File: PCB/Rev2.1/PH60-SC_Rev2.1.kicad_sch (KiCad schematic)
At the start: 48 parts, among them J1 USB_C_Receptacle_USB2.0_14P, J2 Conn_01x02_Pin, J3 Conn_01x02_Pin, U1 nRF52840, U5 LIS2DE12, X1 32.768kHz, X2 Crystal_Generic

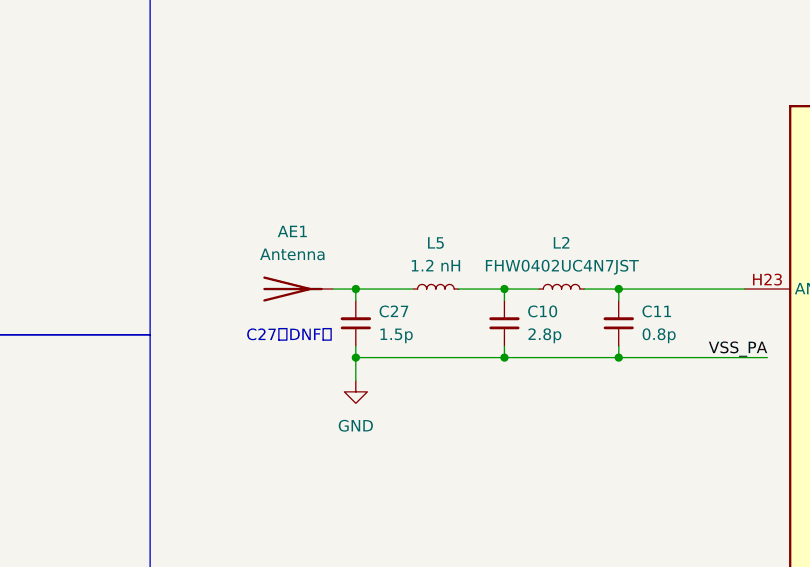
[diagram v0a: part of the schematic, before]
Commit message: 天线设计回退至sc2生产版本
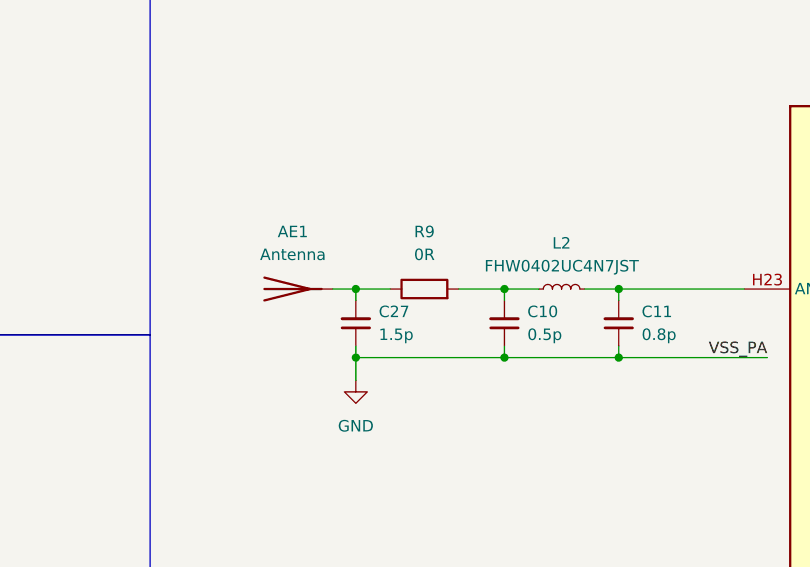
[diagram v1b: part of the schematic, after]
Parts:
- removed L5: 1.2 nH, Inductor_SMD:L_0402_1005Metric, symbol Device:L_Small
- added R9: 0R, Capacitor_SMD:C_0402_1005Metric, symbol Device:R
- C10: value 2.8p -> 0.5p
- C27: now in the parts list
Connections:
- net at AE1.1 (A), C27.2: now also R9.1
- net at C10.2, L2.1: now also R9.2
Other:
- note removed: "C27（DNF）"
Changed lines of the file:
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@@
 		)
 	)
-	(text "C27（DNF）"
-		(exclude_from_sim no)
-		(at 124.714 78.994 0)
-		(effects
-			(font
-				(size 1.27 1.27)
-			)
-		)
-	)
 	(text "ESD"
 		(exclude_from_sim no)
@@
 	)
 	(junction
+		(at 148.59 73.66)
+		(diameter 0)
+		(color 0 0 0 0)
+	)
+	(junction
 		(at 288.29 34.29)
 		(diameter 0)
@@
 		(color 0 0 0 0)
 	)
-	(junction
-		(at 148.59 73.66)
-		(diameter 0)
-		(color 0 0 0 0)
-	)
 	(no_connect
 		(at 241.3 101.6)
@@
 	(wire
 		(pts
-			(xy 143.51 73.66) (xy 148.59 73.66)
-		)
-		(stroke
-			(width 0)
-			(type default)
-		)
-	)
-	(wire
-		(pts
 			(xy 166.37 162.56) (xy 175.26 162.56)
 		)
@@
 	(wire
 		(pts
+			(xy 143.51 73.66) (xy 148.59 73.66)
+		)
+		(stroke
+			(width 0)
+			(type default)
+		)
+	)
+	(wire
+		(pts
 			(xy 298.45 41.91) (xy 298.45 45.72)
 		)
@@
 	(wire
 		(pts
+			(xy 132.08 73.66) (xy 135.89 73.66)
+		)
+		(stroke
+			(width 0)
+			(type default)
+		)
+	)
+	(wire
+		(pts
 			(xy 248.92 182.88) (xy 257.81 182.88)
 		)
@@
 	(wire
 		(pts
-			(xy 132.08 73.66) (xy 138.43 73.66)
-		)
-		(stroke
-			(width 0)
-			(type default)
-		)
-	)
-	(wire
-		(pts
 			(xy 213.36 35.56) (xy 213.36 48.26)
 		)
@@
 	)
 	(symbol
+		(lib_id "Device:R")
+		(at 139.7 73.66 90)
+		(unit 1)
+		(body_style 1)
+		(exclude_from_sim no)
+		(in_bom yes)
+		(on_board yes)
+		(in_pos_files yes)
+		(dnp no)
+		(fields_autoplaced yes)
+		(property "Reference" "R9"
+			(at 139.7 67.31 90)
+			(show_name no)
+			(do_not_autoplace no)
+			(effects
+				(font
+					(size 1.27 1.27)
+				)
+			)
+		)
+		(property "Value" "0R"
+			(at 139.7 69.85 90)
+			(show_name no)
+			(do_not_autoplace no)
+			(effects
+				(font
+					(size 1.27 1.27)
+				)
+			)
+		)
+		(property "Footprint" "Capacitor_SMD:C_0402_1005Metric"
+			(at 139.7 75.438 90)
+			(hide yes)
+			(show_name no)
+			(do_not_autoplace no)
+			(effects
+				(font
+					(size 1.27 1.27)
+				)
+			)
+		)
+		(property "Datasheet" ""
+			(at 139.7 73.66 0)
+			(hide yes)
+			(show_name no)
+			(do_not_autoplace no)
+			(effects
+				(font
+					(size 1.27 1.27)
+				)
+			)
+		)
+		(property "Description" "Resistor"
+			(at 139.7 73.66 0)
+			(hide yes)
+			(show_name no)
+			(do_not_autoplace no)
+			(effects
+				(font
+					(size 1.27 1.27)
+				)
+			)
+		)
+		(pin "2"
+		)
+		(pin "1"
+		)
+		(instances
+			(project "PH60-SC_Rev2.1"
+				(path "/dca0f898-8fdb-4522-a51d-f4f4238906e7"
+					(reference "R9")
+					(unit 1)
+				)
+			)
+		)
+	)
+	(symbol
 		(lib_id "Device:L_Small")
 		(at 283.21 30.48 0)
@@
 			)
 		)
-		(property "Value" "2.8p"
+		(property "Value" "0.5p"
 			(at 151.13 78.7335 0)
 			(show_name no)
@@
 		(body_style 1)
 		(exclude_from_sim no)
-		(in_bom no)
+		(in_bom yes)
 		(on_board yes)
 		(in_pos_files yes)
@@
 					(unit 1)
 				)
-			)
-		)
-	)
-	(symbol
-		(lib_id "Device:L_Small")
-		(at 140.97 73.66 90)
-		(unit 1)
-		(body_style 1)
-		(exclude_from_sim no)
-		(in_bom yes)
-		(on_board yes)
-		(in_pos_files yes)
-		(dnp no)
-		(fields_autoplaced yes)
-		(property "Reference" "L5"
-			(at 140.97 68.58 90)
-			(show_name no)
-			(do_not_autoplace no)
-			(effects
-				(font
-					(size 1.27 1.27)
-				)
-			)
-		)
-		(property "Value" "1.2 nH"
-			(at 140.97 71.12 90)
-			(show_name no)
-			(do_not_autoplace no)
-			(effects
-				(font
-					(size 1.27 1.27)
-				)
-			)
-		)
-		(property "Footprint" "Inductor_SMD:L_0402_1005Metric"
-			(at 140.97 73.66 0)
-			(hide yes)
-			(show_name no)
-			(do_not_autoplace no)
-			(effects
-				(font
-					(size 1.27 1.27)
-				)
-			)
-		)
-		(property "Datasheet" ""
-			(at 140.97 73.66 0)
-			(hide yes)
-			(show_name no)
-			(do_not_autoplace no)
-			(effects
-				(font
-					(size 1.27 1.27)
-				)
-			)
-		)
-		(property "Description" "Inductor, small symbol"
-			(at 140.97 73.66 0)
-			(hide yes)
-			(show_name no)
-			(do_not_autoplace no)
-			(effects
-				(font
-					(size 1.27 1.27)
-				)
-			)
-		)
-		(pin "2"
-		)
-		(pin "1"
-		)
-		(instances
-			(project "PH60-SC_Rev2.1"
-				(path "/dca0f898-8fdb-4522-a51d-f4f4238906e7"
-					(reference "L5")
-					(unit 1)
-				)
